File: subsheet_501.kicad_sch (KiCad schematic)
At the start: 11 parts, among them U509 74LS244_PHY, U510 74LS244_PHY, U511 74LS373_PHY, U512 74LS244_PHY

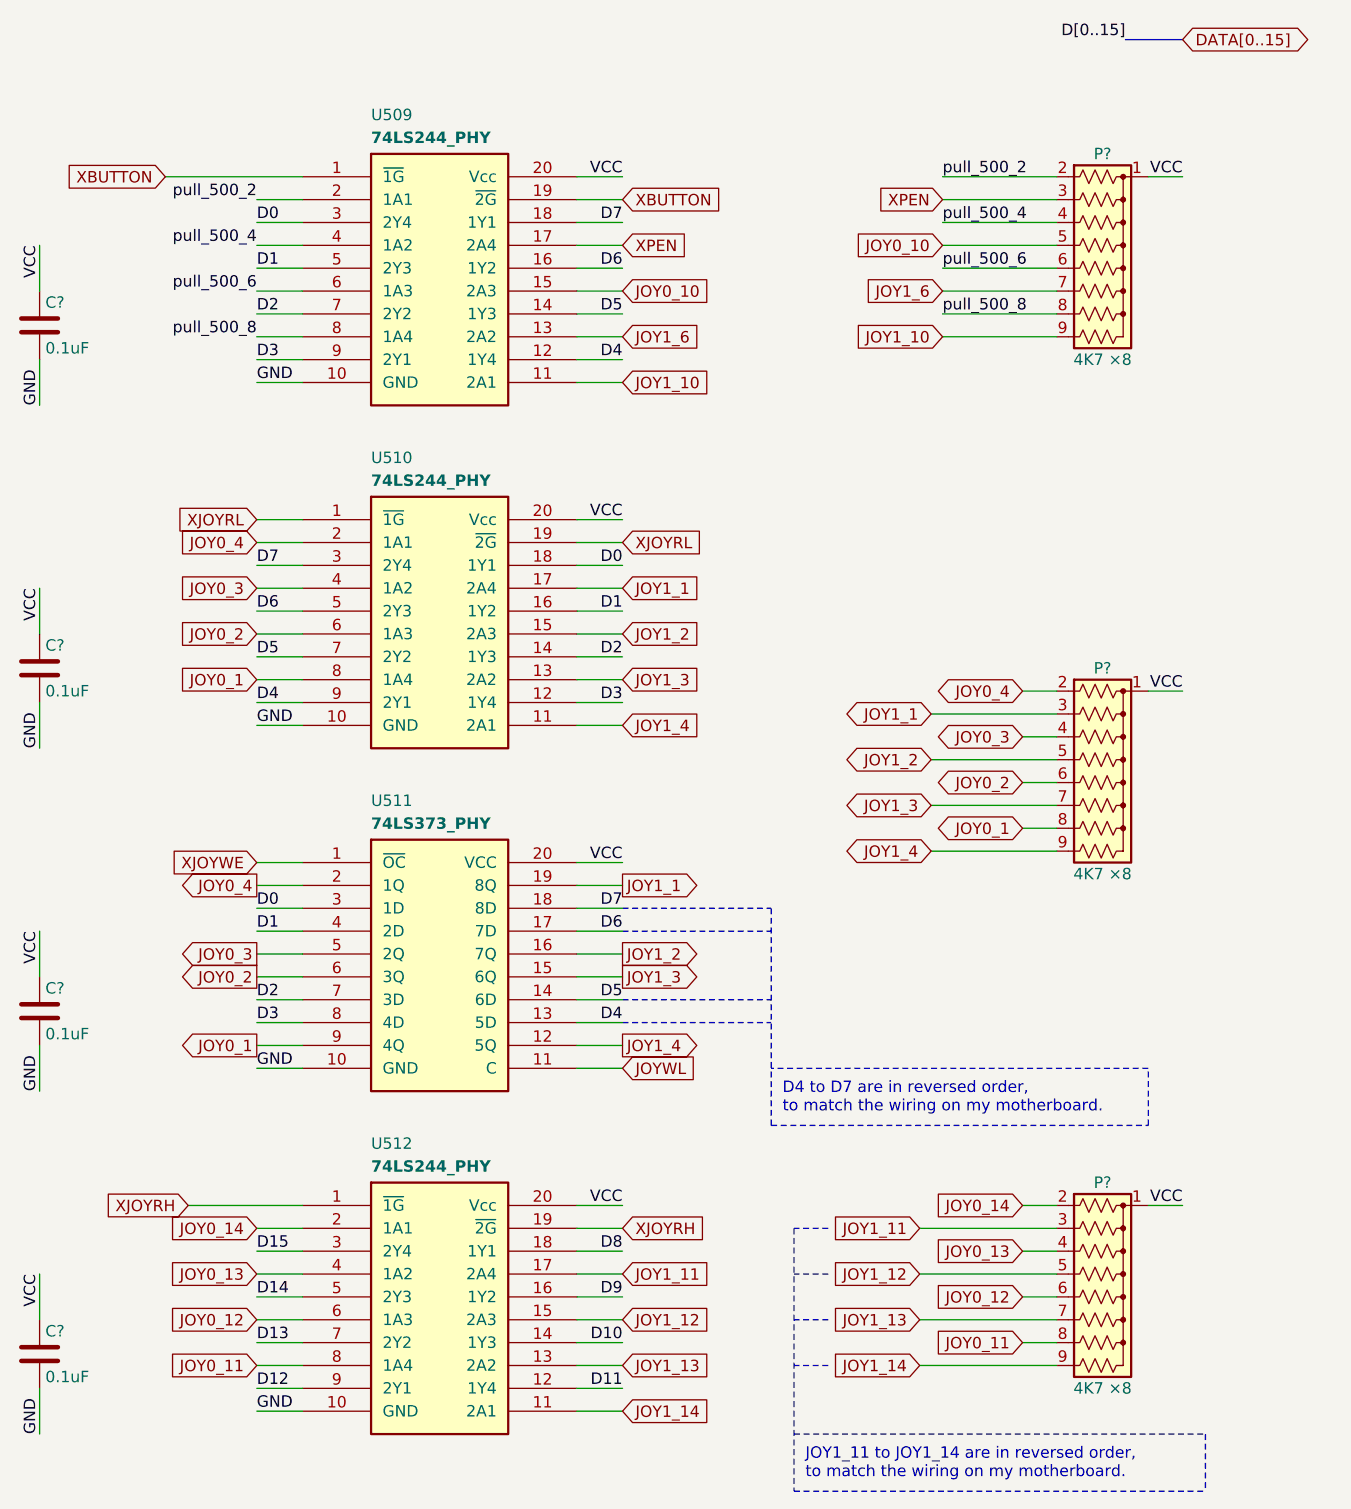
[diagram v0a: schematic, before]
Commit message: Resolves #3 : [schematic] annotate video port with signal name
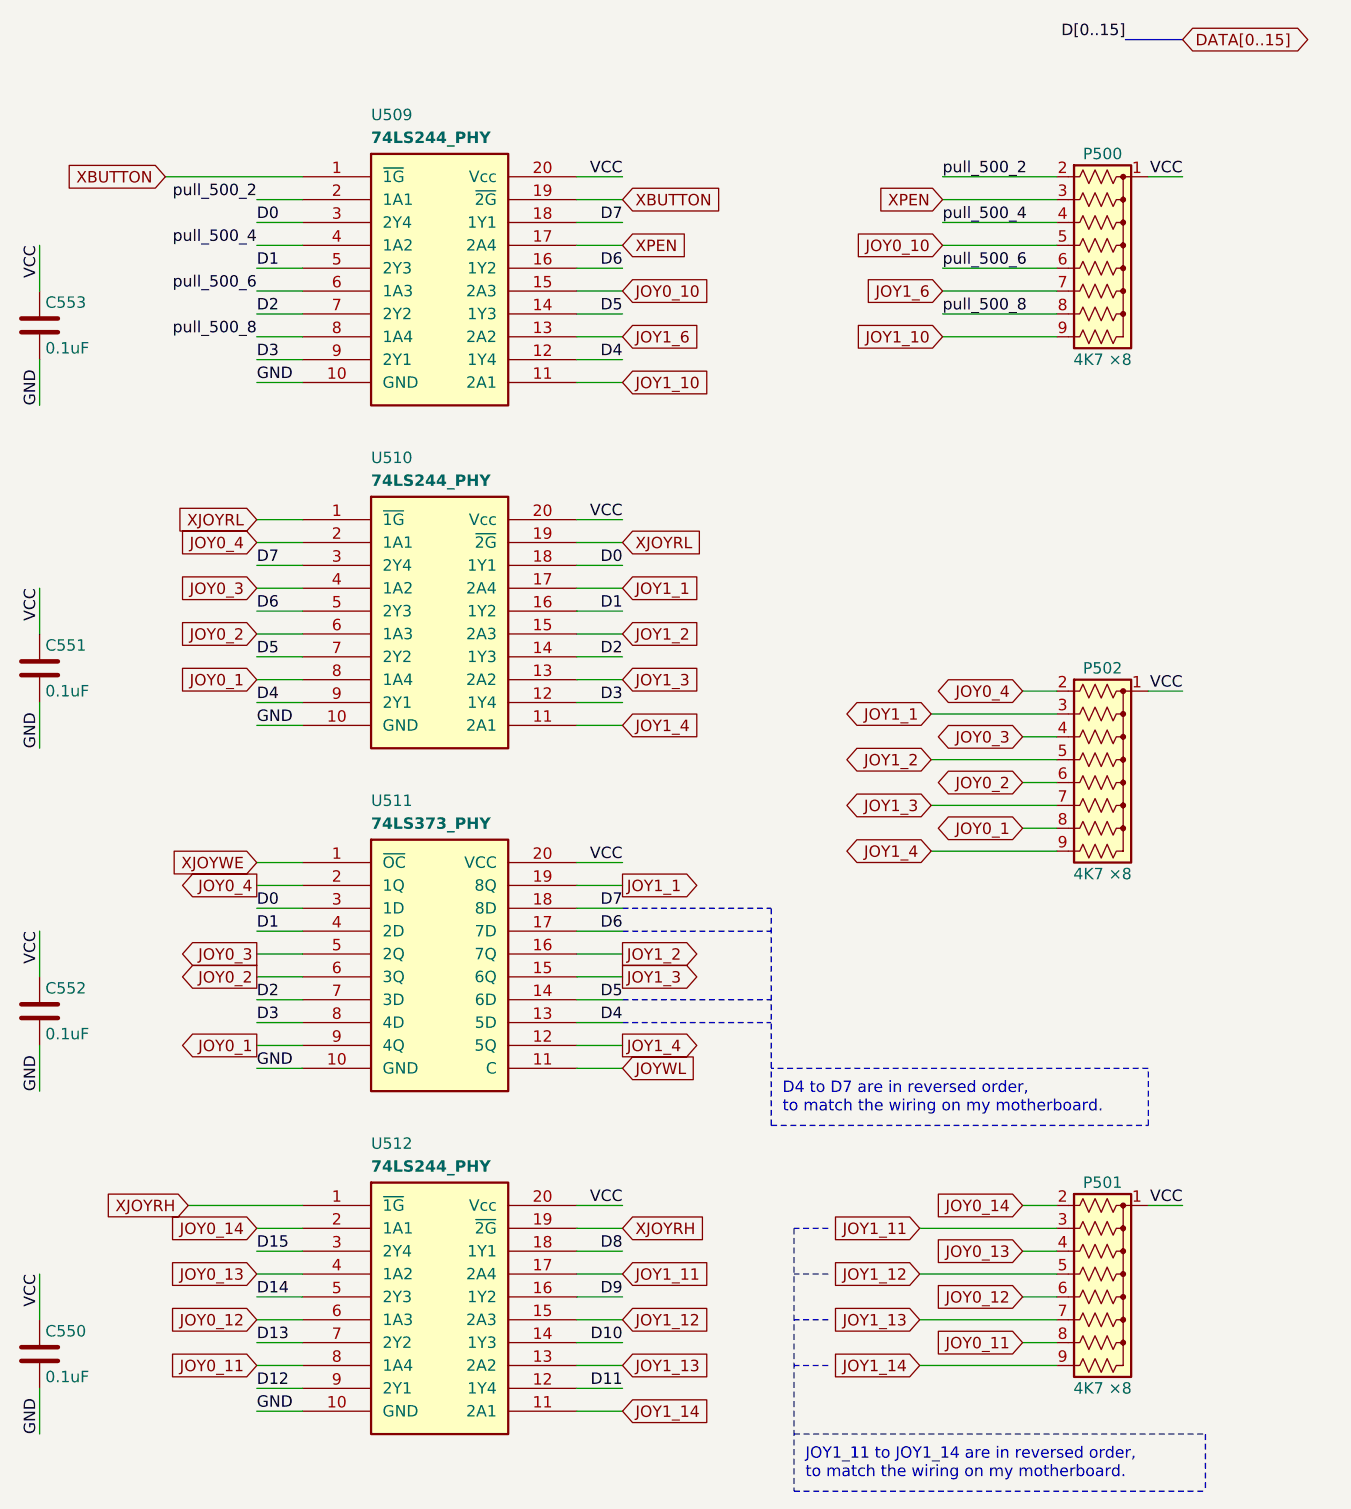
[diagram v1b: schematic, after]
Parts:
- gave numbers to parts that had none: 7
